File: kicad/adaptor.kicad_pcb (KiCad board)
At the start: 2 copper layers, 62.1 x 40.1 mm, 4 parts

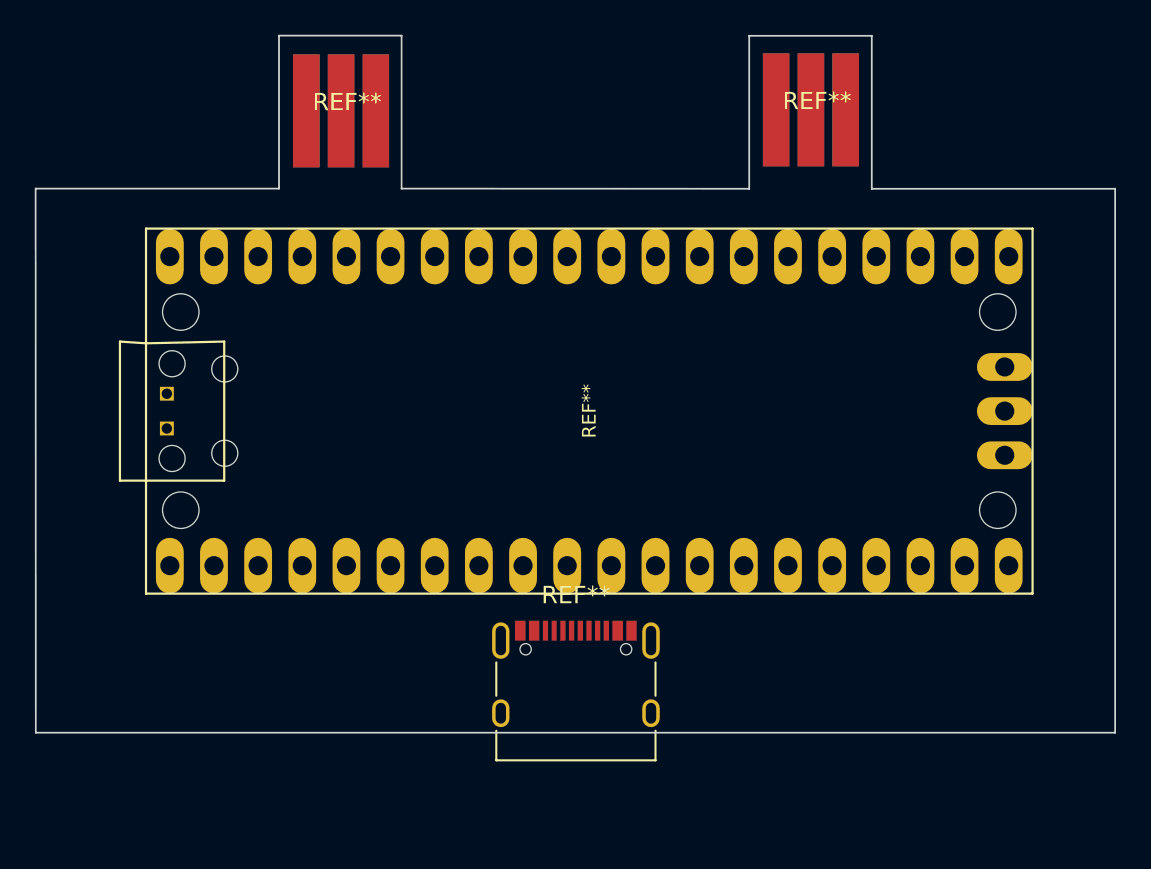
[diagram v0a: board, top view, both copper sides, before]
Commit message: multithreaded pio joybus to avoid stalling the usb descriptors running on core 0
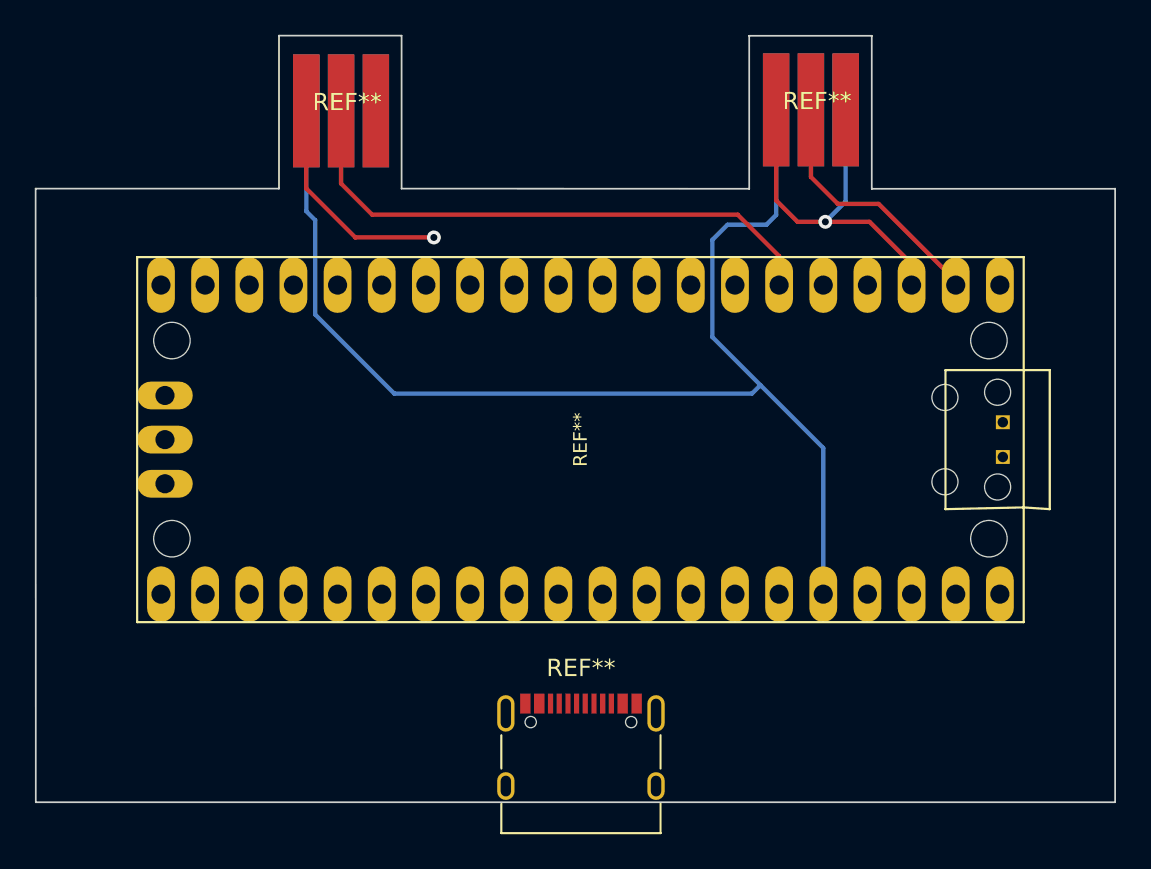
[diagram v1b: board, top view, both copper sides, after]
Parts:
- moved REF** 4.20 mm to (109.7, 110.0)
- moved REF** 1.72 mm to (109.7, 91.1), turned to -90 degrees
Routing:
- net (no net): track 0.00 -> 156.3 mm, vias 0 -> 2
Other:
- board size 62.1 x 40.1 mm -> 62.1 x 44.1 mm
